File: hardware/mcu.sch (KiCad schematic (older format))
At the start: 29 parts, among them P1 CONN_01X16, SW1 SPST, SW2 SPST, U1 ISO1050, U2 LPC11C14, U3 MCP2515_TSSOP, U4 ISO1050

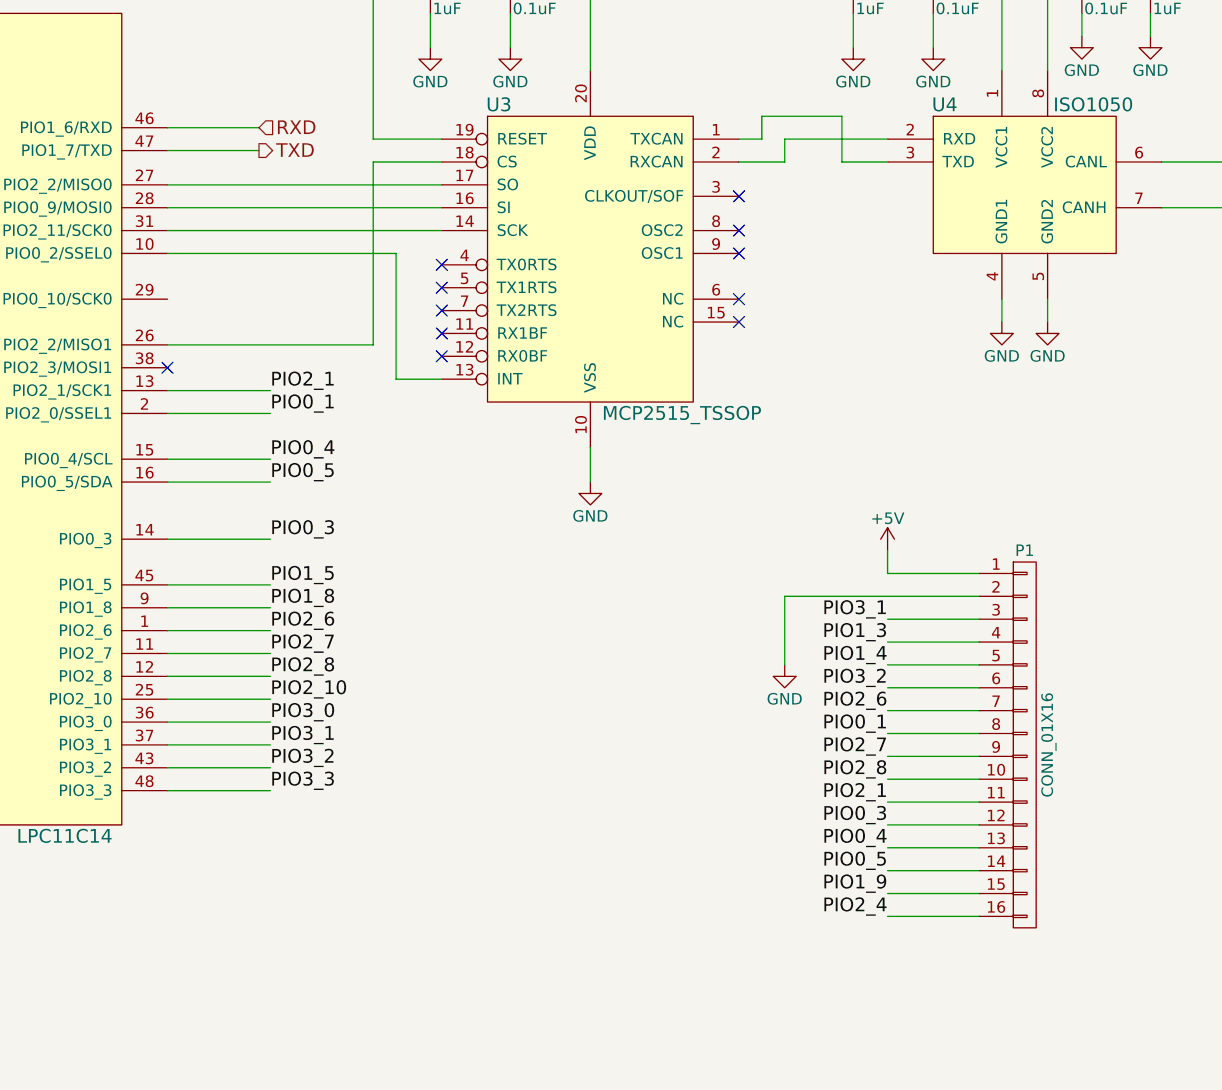
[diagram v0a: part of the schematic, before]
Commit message: updadted pinout and buttons
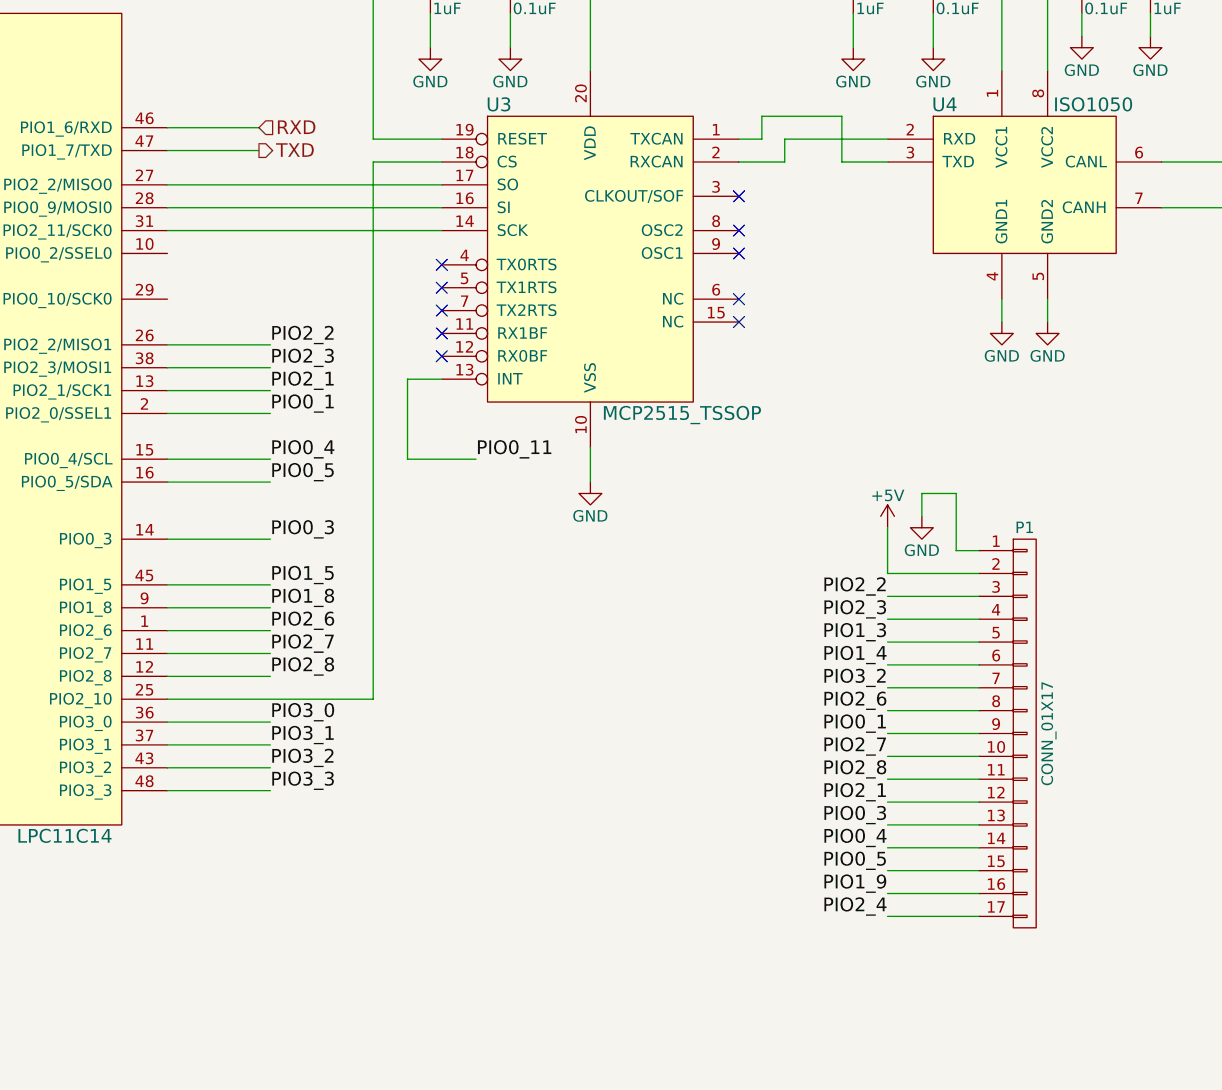
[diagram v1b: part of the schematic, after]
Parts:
- removed P1: CONN_01X16, Pin_Headers:Pin_Header_Straight_1x16, symbol CONN_01X16
- added P1: CONN_01X17, Pin_Headers:Pin_Header_Straight_1x17, symbol CONN_01X17
- SW2: footprint Buttons_Switches_SMD:SW_SPST_FSMSM -> Buttons_Switches_ThroughHole:SW_Micro_SPST
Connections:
- net PIO2_10 is gone; now on an unnamed net: U2.25 (PIO2_10)
- net +5V: now also P1.2 (P2)
- net GND: now also P1.1 (P1)
- net PIO0_1: now also P1.9 (P9)
- net PIO0_11: now also U3.13 (INT)
- net PIO0_3: now also P1.13 (P13)
- net PIO0_4: now also P1.14 (P14)
- net PIO0_5: now also P1.15 (P15)
- net PIO1_3: now also P1.5 (P5)
- net PIO1_4: now also P1.6 (P6)
- net PIO1_9: now also P1.16 (P16)
- net PIO2_1: now also P1.12 (P12)
- net PIO2_4: now also P1.17 (P17)
- net PIO2_6: now also P1.8 (P8)
- net PIO2_7: now also P1.10 (P10)
- net PIO2_8: now also P1.11 (P11)
- net PIO3_2: now also P1.7 (P7)
- net at U2.10 (PIO0_2/SSEL0): no longer U3.13 (INT)
- net at U3.18 (CS): no longer U2.26 (PIO2_2/MISO1)
- net PIO2_3: now reaches U2.38 (PIO2_3/MOSI1)
- net PIO2_3: now also P1.4 (P4)
- new net PIO2_2: P1.3 (P3), U2.26 (PIO2_2/MISO1)
- no-connect marks 13 -> 12
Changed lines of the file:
@@
 	6150 3000 7350 3000
 Wire Wire Line
-	7350 3650 7150 3650
-Wire Wire Line
-	7150 3650 7150 3100
-Wire Wire Line
-	7150 3100 6150 3100
-Wire Wire Line
-	7050 2700 7050 3500
+	7050 5050 7050 2700
 Wire Wire Line
 	7050 2700 7350 2700
-Wire Wire Line
-	7050 3500 6150 3500
 $Comp
 L ISO1050 U4
@@
 F 0 "SW2" H 2850 3050 50  0000 C CNN
 F 1 "SPST" H 2850 2850 50  0000 C CNN
-F 2 "Buttons_Switches_SMD:SW_SPST_FSMSM" H 2850 2950 60  0001 C CNN
+F 2 "Buttons_Switches_ThroughHole:SW_Micro_SPST" H 2850 2950 60  0001 C CNN
 F 3 "" H 2850 2950 60  0000 C CNN
 	1    2850 2950
@@
 	2050 2950 2050 2550
 Connection ~ 2050 2550
-$Comp
-L CONN_01X16 P1
-U 1 1 5619BB5F
-P 9900 5250
-F 0 "P1" H 9900 6100 50  0000 C CNN
-F 1 "CONN_01X16" V 10000 5250 50  0000 C CNN
-F 2 "Pin_Headers:Pin_Header_Straight_1x16" H 9900 5250 60  0001 C CNN
-F 3 "" H 9900 5250 60  0000 C CNN
-	1    9900 5250
-	1    0    0    -1
-$EndComp
-Wire Wire Line
-	9700 4500 9300 4500
-Wire Wire Line
-	8850 4600 9700 4600
 Wire Wire Line
 	9700 4700 9300 4700
@@
 	6150 4950 6600 4950
 Wire Wire Line
-	6150 5050 6600 5050
+	6150 5050 7050 5050
 Wire Wire Line
 	6150 5150 6600 5150
@@
 Text Label 6600 4950 0    60   ~ 0
 PIO2_8
-Text Label 6600 5050 0    60   ~ 0
-PIO2_10
 Text Label 6600 5150 0    60   ~ 0
 PIO3_0
@@
 NoConn ~ 3500 2650
 NoConn ~ 3500 2750
-NoConn ~ 6150 3600
 Wire Wire Line
 	7350 2600 7050 2600
@@
 Text Label 9300 4800 2    60   ~ 0
 PIO1_3
-Text Label 9300 4700 2    60   ~ 0
-PIO3_1
-Wire Wire Line
-	8850 4600 8850 4900
-$Comp
-L GND #PWR030
-U 1 1 56209D40
-P 8850 4900
-F 0 "#PWR030" H 8850 4650 50  0001 C CNN
-F 1 "GND" H 8850 4750 50  0000 C CNN
-F 2 "" H 8850 4900 60  0000 C CNN
-F 3 "" H 8850 4900 60  0000 C CNN
-	1    8850 4900
-	1    0    0    -1
-$EndComp
 $Comp
 L +5V #PWR031
 U 1 1 56209D87
-P 9300 4400
-F 0 "#PWR031" H 9300 4250 50  0001 C CNN
-F 1 "+5V" H 9300 4540 50  0000 C CNN
-F 2 "" H 9300 4400 60  0000 C CNN
-F 3 "" H 9300 4400 60  0000 C CNN
-	1    9300 4400
-	1    0    0    -1
-$EndComp
-Wire Wire Line
-	9300 4500 9300 4400
+P 9300 4300
+F 0 "#PWR031" H 9300 4150 50  0001 C CNN
+F 1 "+5V" H 9300 4440 50  0000 C CNN
+F 2 "" H 9300 4300 60  0000 C CNN
+F 3 "" H 9300 4300 60  0000 C CNN
+	1    9300 4300
+	1    0    0    -1
+$EndComp
+Wire Wire Line
+	9300 4300 9300 4500
+Wire Wire Line
+	6150 3500 6600 3500
+Text Label 6600 3500 0    60   ~ 0
+PIO2_2
+Wire Wire Line
+	6150 3600 6600 3600
+Text Label 6600 3600 0    60   ~ 0
+PIO2_3
+Text Label 7500 4000 0    60   ~ 0
+PIO0_11
+Wire Wire Line
+	7350 3650 7200 3650
+Wire Wire Line
+	7200 3650 7200 4000
+Wire Wire Line
+	7200 4000 7500 4000
+Text Label 9300 4700 2    60   ~ 0
+PIO2_3
+$Comp
+L CONN_01X17 P1
+U 1 1 5622AEB7
+P 9900 5200
+F 0 "P1" H 9900 6100 50  0000 C CNN
+F 1 "CONN_01X17" V 10000 5200 50  0000 C CNN
+F 2 "Pin_Headers:Pin_Header_Straight_1x17" H 9900 5200 60  0001 C CNN
+F 3 "" H 9900 5200 60  0000 C CNN
+	1    9900 5200
+	1    0    0    -1
+$EndComp
+Text Label 9300 4600 2    60   ~ 0
+PIO2_2
+Wire Wire Line
+	9300 4600 9700 4600
+Wire Wire Line
+	9300 4500 9700 4500
+Wire Wire Line
+	9700 4400 9600 4400
+Wire Wire Line
+	9600 4400 9600 4150
+Wire Wire Line
+	9600 4150 9450 4150
+Wire Wire Line
+	9450 4150 9450 4250
+$Comp
+L GND #PWR?
+U 1 1 5622B689
+P 9450 4250
+F 0 "#PWR?" H 9450 4000 50  0001 C CNN
+F 1 "GND" H 9450 4100 50  0000 C CNN
+F 2 "" H 9450 4250 60  0000 C CNN
+F 3 "" H 9450 4250 60  0000 C CNN
+	1    9450 4250
+	1    0    0    -1
+$EndComp
 $EndSCHEMATC

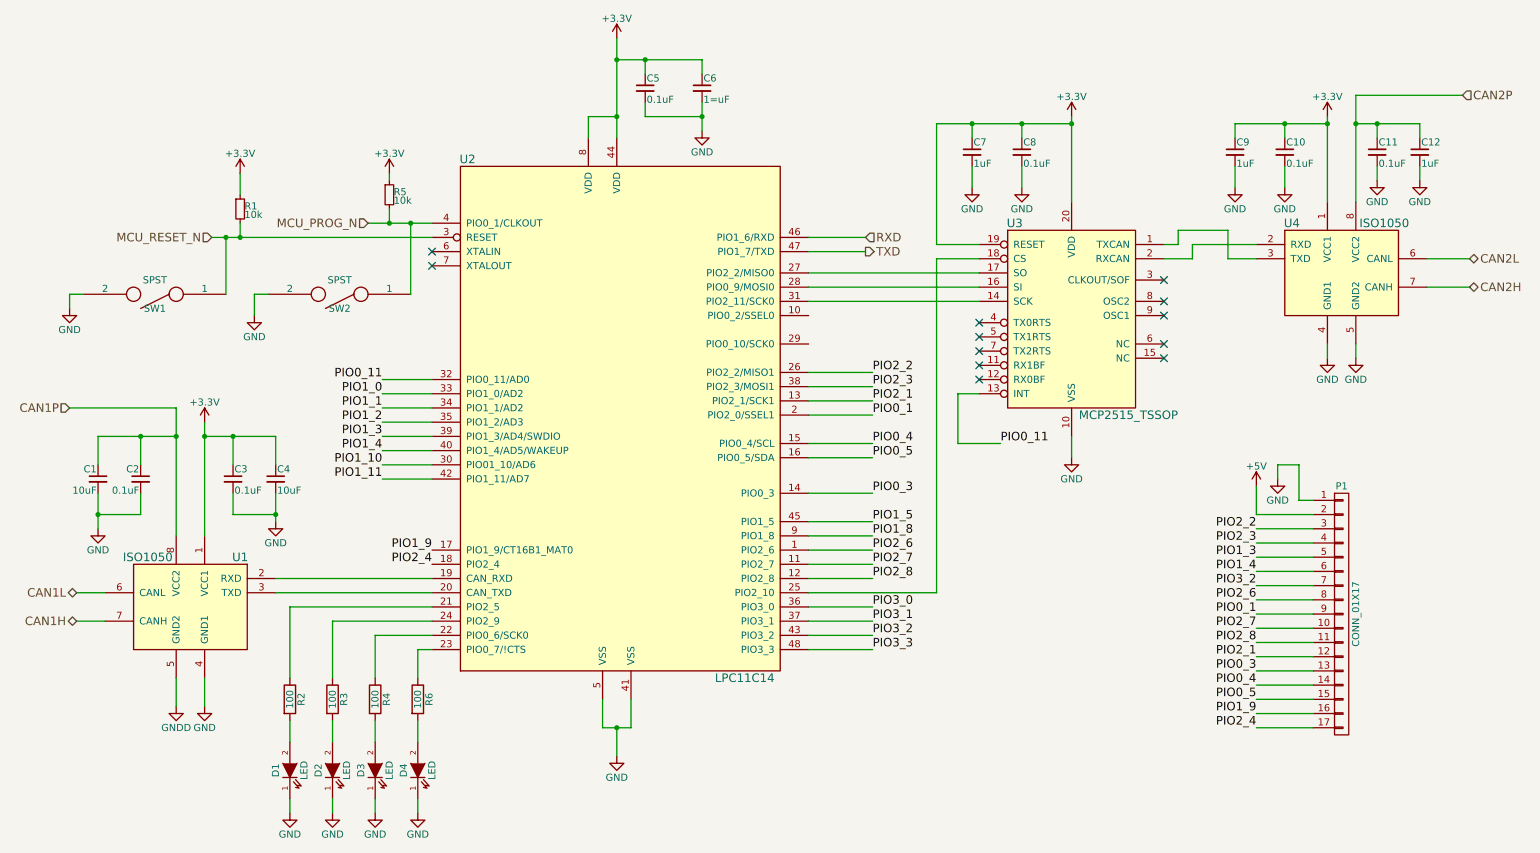
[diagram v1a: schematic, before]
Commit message: devboard fixed, added LED, Added Capacitor, Changed CAN chips
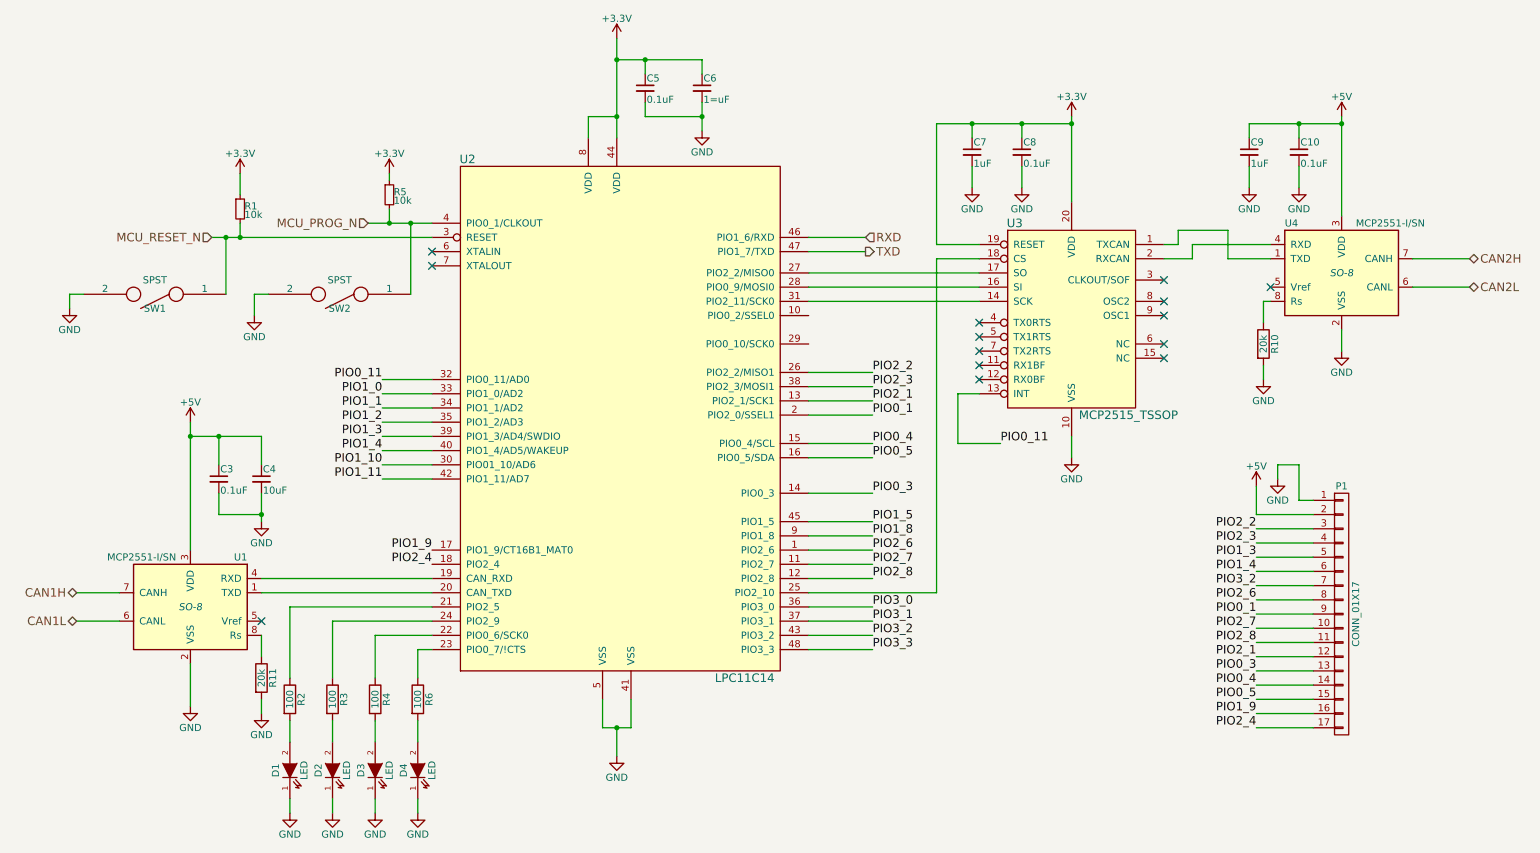
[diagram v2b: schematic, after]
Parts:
- removed C1: 10uF, Capacitors_SMD:C_0805_HandSoldering, symbol C_Small
- removed C11, C2: 0.1uF, Capacitors_SMD:C_0603_HandSoldering, symbol C_Small
- removed C12: 1uF, Capacitors_SMD:C_0805_HandSoldering, symbol C_Small
- removed U1, U4: ISO1050, Housings_SSOP:MSOP-8_3x3mm_Pitch0.65mm, symbol ISO1050
- added R10, R11: 20k, Resistors_SMD:R_0603_HandSoldering, symbol R
- added U1, U4: MCP2551-I/SN, SO-8, symbol MCP2551-I/SN
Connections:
- net +3V3: no longer C10.1, C3.1, C4.1, C9.1
- net +5V: now also C10.1, C3.1, C4.1, C9.1, U1.3 (VDD), U4.3 (VDD)
- net CAN1H: now also U1.7 (CANH)
- net CAN1L: now also U1.6 (CANL)
- net CAN2H: now also U4.7 (CANH)
- net CAN2L: now also U4.6 (CANL)
- net GND: now also R10.2, R11.2, U1.2 (VSS), U4.2 (VSS)
- net at U2.19 (CAN_RXD): now also U1.4 (RXD)
- net at U2.20 (CAN_TXD): now also U1.1 (TXD)
- net at U3.1 (TXCAN): now also U4.1 (TXD)
- net at U3.2 (RXCAN): now also U4.4 (RXD)
- new net: R10.1, U4.8 (Rs)
- new net: R11.1, U1.8 (Rs)
- no-connect marks 12 -> 14
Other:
- moved on the sheet: C10, C3, C4, C9

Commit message: Changed to add a 3.3 volt connection
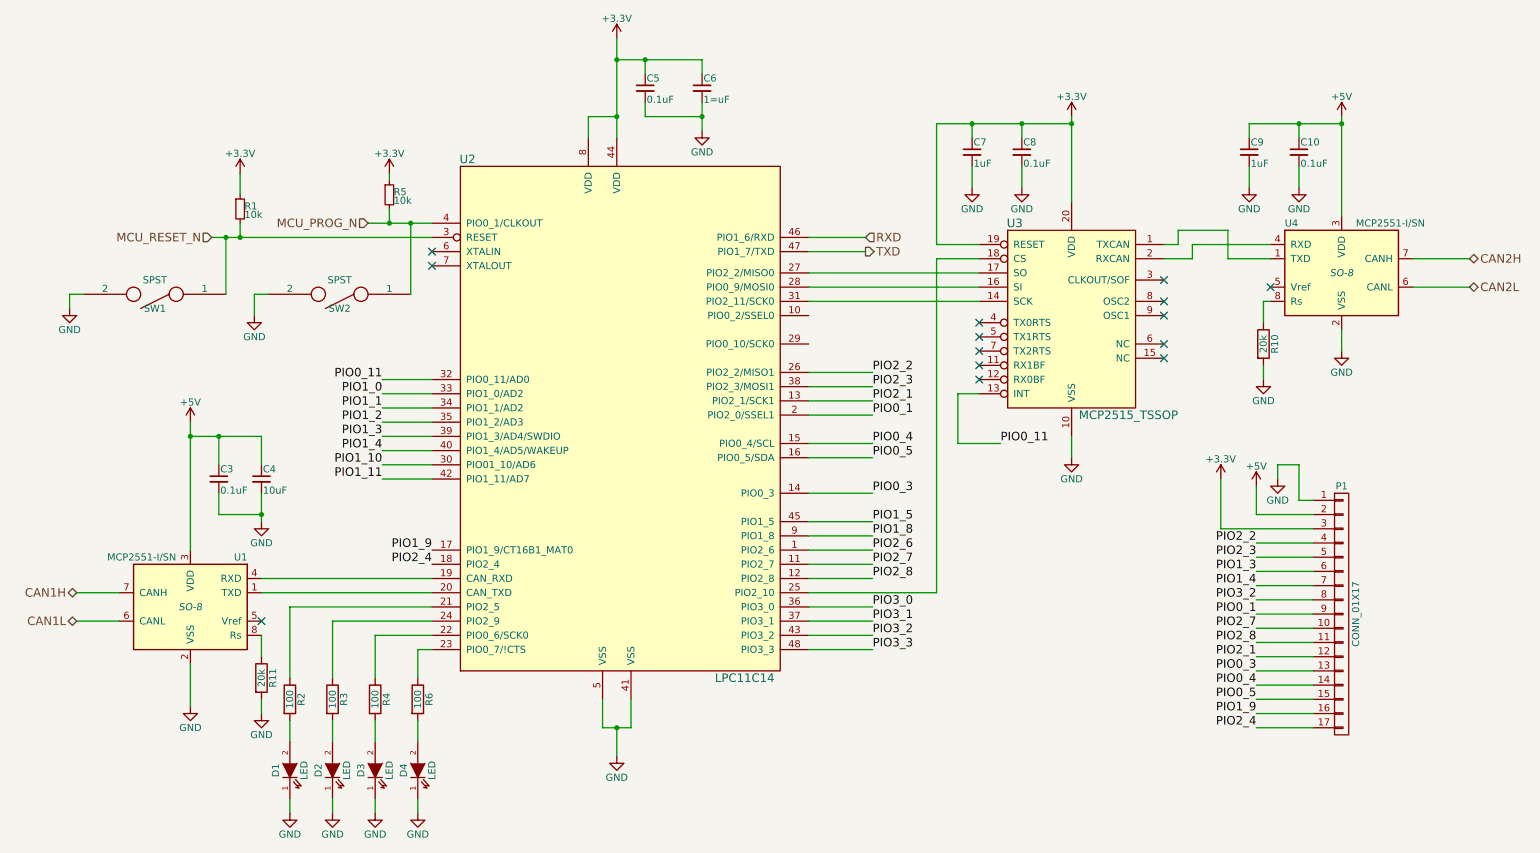
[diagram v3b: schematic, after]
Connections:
- net +3V3: now also P1.3 (P3)
- net PIO1_3: now also P1.6 (P6); no longer P1.5 (P5)
- net PIO1_4: now also P1.7 (P7); no longer P1.6 (P6)
- net PIO2_2: now also P1.4 (P4); no longer P1.3 (P3)
- net PIO2_3: now also P1.5 (P5); no longer P1.4 (P4)
- net PIO2_6: no longer P1.8 (P8)
- net PIO3_2: now also P1.8 (P8); no longer P1.7 (P7)
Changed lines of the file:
@@
 Text Label 6600 3800 0    60   ~ 0
 PIO0_1
-Text Label 9300 5100 2    60   ~ 0
-PIO2_6
 Text Label 9300 5200 2    60   ~ 0
 PIO0_1
+Text Label 9300 5100 2    60   ~ 0
+PIO3_2
 Text Label 9300 5000 2    60   ~ 0
-PIO3_2
+PIO1_4
 Text Label 9300 4900 2    60   ~ 0
-PIO1_4
-Text Label 9300 4800 2    60   ~ 0
 PIO1_3
 $Comp
@@
 Text Label 7500 4000 0    60   ~ 0
 PIO0_11
-Text Label 9300 4700 2    60   ~ 0
+Text Label 9300 4800 2    60   ~ 0
 PIO2_3
 $Comp
@@
 	1    0    0    -1
 $EndComp
-Text Label 9300 4600 2    60   ~ 0
+Text Label 9300 4700 2    60   ~ 0
 PIO2_2
 $Comp
@@
 	4600 1850 4600 1700
 Wire Wire Line
-	4600 1700 4800 1700
+	4800 1700 4600 1700
 Wire Wire Line
 	4800 1150 4800 1850
@@
 	7200 4000 7500 4000
 Wire Wire Line
-	9300 4600 9700 4600
+	9050 4600 9700 4600
 Wire Wire Line
 	9300 4500 9700 4500
@@
 	1    0    0    -1
 $EndComp
+$Comp
+L +3.3V #PWR?
+U 1 1 56969D5D
+P 9050 4250
+F 0 "#PWR?" H 9050 4100 50  0001 C CNN
+F 1 "+3.3V" H 9050 4390 50  0000 C CNN
+F 2 "" H 9050 4250 50  0000 C CNN
+F 3 "" H 9050 4250 50  0000 C CNN
+	1    9050 4250
+	1    0    0    -1
+$EndComp
+Wire Wire Line
+	9050 4600 9050 4250
 $EndSCHEMATC
